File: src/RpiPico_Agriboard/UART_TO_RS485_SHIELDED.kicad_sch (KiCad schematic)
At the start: 11 parts, among them U8 TP8485E-SR

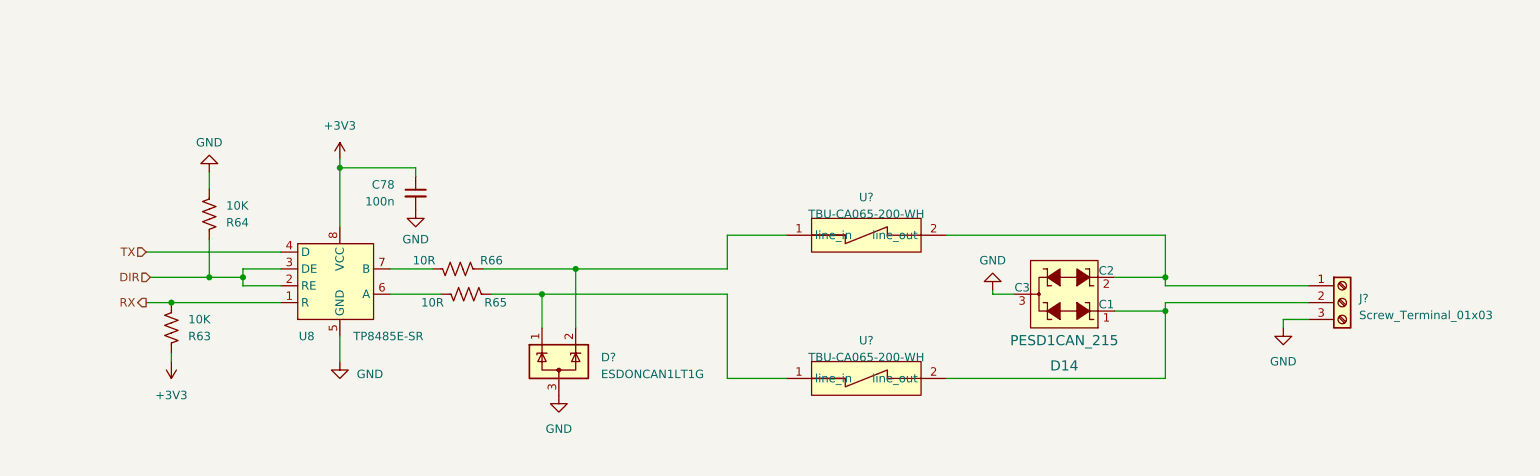
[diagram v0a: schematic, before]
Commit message: Revert "schematic updates completed"
This reverts commit 0124993096667d53f20fd59dec80d3f5a1efcd43.
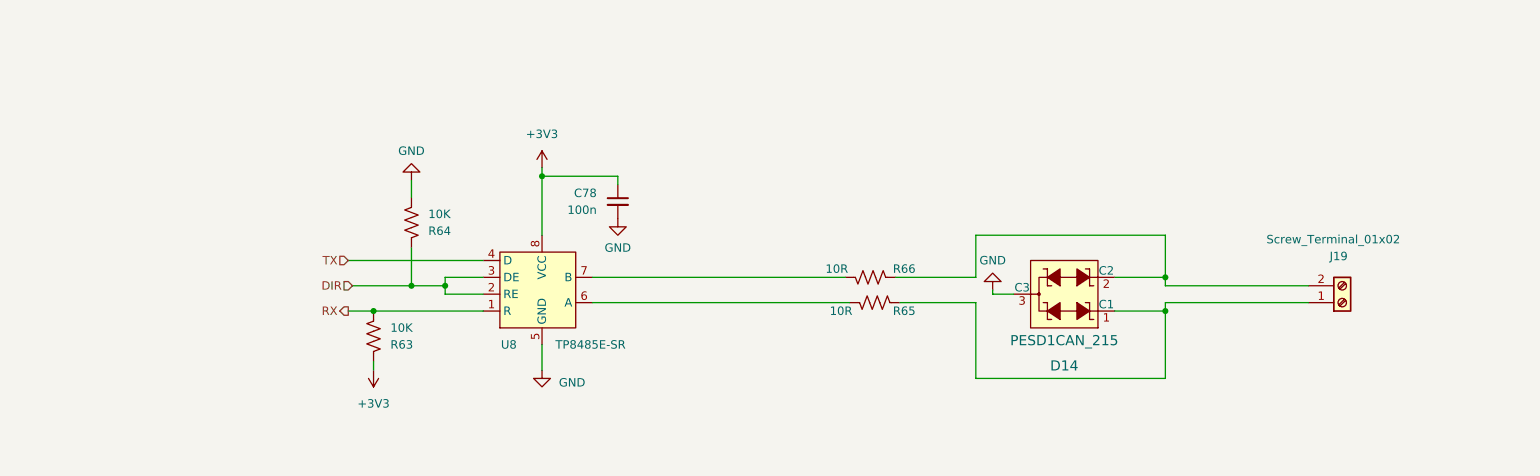
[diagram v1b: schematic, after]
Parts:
- removed D?: ESDONCAN1LT1G, Package_TO_SOT_SMD:SOT-23, symbol Power_Protection:SP0502BAHT
- removed J?: Screw_Terminal_01x03, symbol Connector:Screw_Terminal_01x03
- removed U? (x2): TBU-CA065-200-WH, MACHADA_footprints:TBU-CA065-200-WH, symbol MCD_General:TBU-CA065-200-WH
- added J19: Screw_Terminal_01x02, TerminalBlock_Phoenix:TerminalBlock_Phoenix_PT-1,5-2-3.5-H_1x02_P3.50mm_Horizontal, symbol Connector:Screw_Terminal_01x02
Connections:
- net at R65.2: now also D14.1 (C1), J19.1 (Pin_1)
- net at R66.2: now also D14.2 (C2), J19.2 (Pin_2)
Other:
- moved on the sheet: C78, R63, R64, R65, R66, U8

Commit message: schematic updates completed
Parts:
- removed J19: Screw_Terminal_01x02, TerminalBlock_Phoenix:TerminalBlock_Phoenix_PT-1,5-2-3.5-H_1x02_P3.50mm_Horizontal, symbol Connector:Screw_Terminal_01x02
- added D?: ESDONCAN1LT1G, Package_TO_SOT_SMD:SOT-23, symbol Power_Protection:SP0502BAHT
- added J?: Screw_Terminal_01x03, symbol Connector:Screw_Terminal_01x03
- added U? (x2): TBU-CA065-200-WH, MACHADA_footprints:TBU-CA065-200-WH, symbol MCD_General:TBU-CA065-200-WH
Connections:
- net GND: now also D?.3 (A), J?.3 (Pin_3)
- net at R65.2: now also D?.1 (K), U?.1 (line_in); no longer D14.1 (C1)
- net at R66.2: now also D?.2 (K), U?.1 (line_in); no longer D14.2 (C2)
- new net: D14.2 (C2), J?.1 (Pin_1), U?.2 (line_out)
- new net: D14.1 (C1), J?.2 (Pin_2), U?.2 (line_out)
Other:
- moved on the sheet: C78, R63, R64, R65, R66, U8

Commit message: schematic updates completed
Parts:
- gave numbers to parts that had none: 4
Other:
- moved on the sheet: C78, R63, R64

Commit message: rs485 updates and layout updates
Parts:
- added R73: 100K, Resistor_SMD:R_0402_1005Metric, symbol Device:R_US
- added R74: 120R, Resistor_SMD:R_0402_1005Metric, symbol Device:R_US
- R64: value 10K -> 100K
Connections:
- net +3V3: now also R73.1
- net at R65.1, U8.6 (A): now also R74.1
- net at R66.1, U8.7 (B): now also R74.2
- net DIR renamed DE
- net DE: no longer U8.2 (RE)
- new net RE: R73.2, U8.2 (RE)
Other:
- moved on the sheet: C78, D17, R63, R64, R65, R66

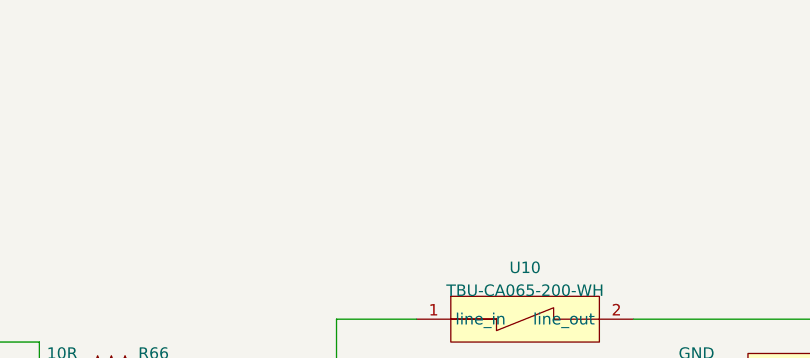
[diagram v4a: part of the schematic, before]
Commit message: complete board update and routing
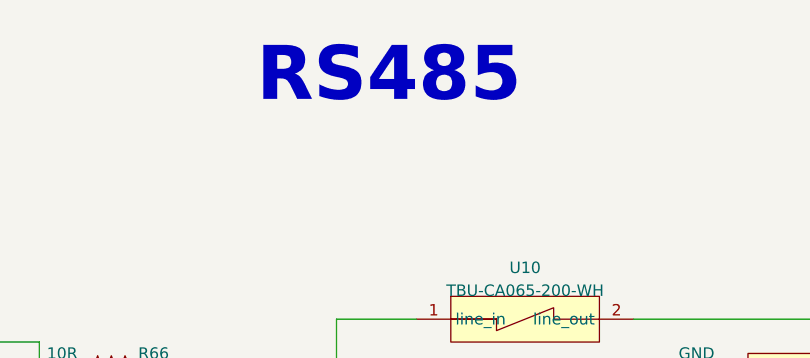
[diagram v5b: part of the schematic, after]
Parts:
- J19: footprint (none) -> TerminalBlock_Phoenix:TerminalBlock_Phoenix_PT-1,5-3-3.5-H_1x03_P3.50mm_Horizontal
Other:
- note added: "RS485"
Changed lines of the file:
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@@
     (stroke (width 0) (type default))
+  )
+  (text "RS485" (at 147.32 42.545 0)
+    (effects (font (face "Agency FB") (size 6 6) bold) (justify left bottom))
   )
   (hierarchical_label "RE" (shape input) (at 71.12 73.66 180) (fields_autoplaced)
@@
       (effects (font (size 1.27 1.27)) (justify left))
     )
-    (property "Footprint" "" (at 248.92 76.2 0)
-      (effects (font (size 1.27 1.27)) hide)
-    )
+    (property "Footprint" "TerminalBlock_Phoenix:TerminalBlock_Phoenix_PT-1,5-3-3.5-H_1x03_P3.50mm_Horizontal" (at 248.92 76.2 0)
+      (effects (font (size 1.27 1.27)) hide)
+    )
